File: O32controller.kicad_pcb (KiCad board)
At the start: 4 copper layers, 27 x 27 mm, 64 parts, among them J1 Conn_01x08_MountingPin, J2 BATT+, J3 BATT-, J4 Motor Connection, J5 Motor Connection, J6 Motor Connection, J7 BATT+, J8 BATT-, Q1 DMM0022A, Q2 DMM0022A, Q3 DMM0022A, U1 AS5047D, U2 STSPIN32F0A

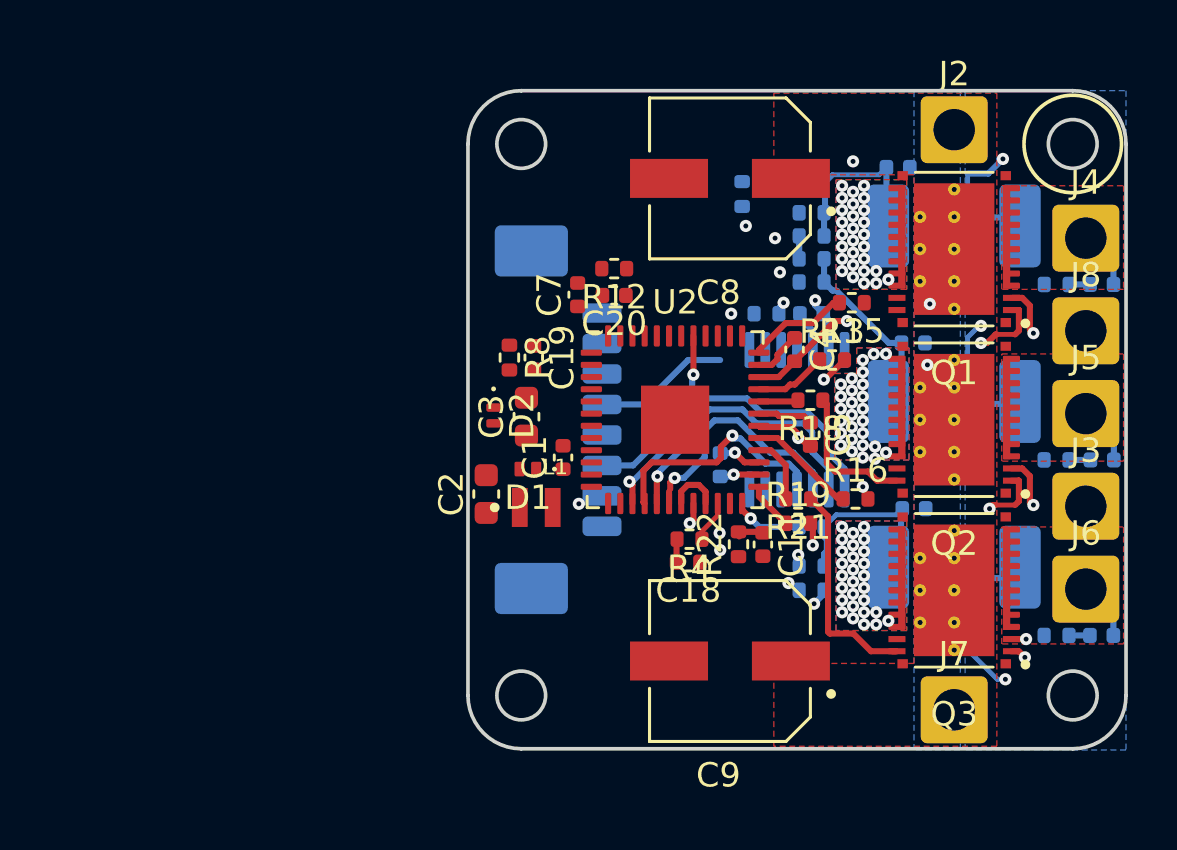
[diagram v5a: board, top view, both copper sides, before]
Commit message: just need to figure out gpio and buck
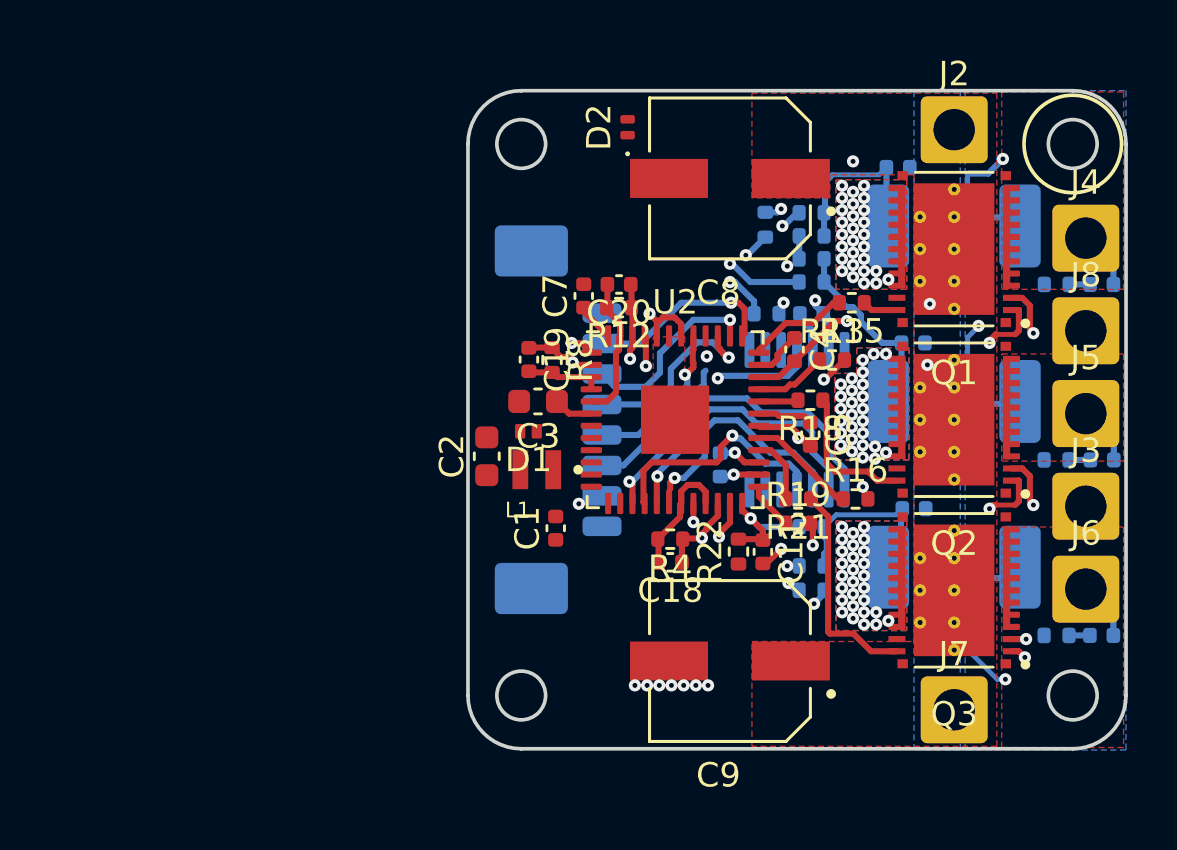
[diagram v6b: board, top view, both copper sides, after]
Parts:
- Q1, Q2, Q3: value DMM0022A -> CSD88584Q5DCT
- moved D2 13.0 mm to (43.0, 38.0), turned to 90 degrees
- moved C1 2.92 mm to (40.1, 54.5)
- moved R8 1.75 mm to (40.0, 47.5)
- moved R12 1.61 mm to (42.7, 45.4)
- moved R3 1.58 mm to (48.7, 42.0)
- moved L1 1.55 mm to (39.3, 52.0), turned to 180 degrees
- moved C2 1.55 mm to (37.3, 51.5)
- moved D1 1.55 mm to (39.0, 50.5)
- moved R4 0.79 mm to (44.8, 54.9)
- moved C3 0.79 mm to (39.4, 49.2), turned to 180 degrees
- moved C18 0.74 mm to (44.8, 55.9)
- moved C20 0.49 mm to (42.7, 44.5)
- moved C11 0.30 mm to (48.6, 55.4)
- moved R22 0.30 mm to (47.6, 55.4)
- moved C7 0.25 mm to (41.2, 44.9)
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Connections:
- J1 pad 2: I2C_SCL -> unconnected-(J1-Pad2)
- J1 pad 3: I2C_SDA -> I2C_SCL
- J1 pad 4: /GPIO_PA15 -> I2C_SDA
- J1 pad 5: SWD_CLK -> /GPIO_PA15
- J1 pad 6: SWD_IO -> SWD_CLK
- J1 pad 7: unconnected-(J1-Pad7) -> SWD_IO
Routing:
- net +3.3V: track 2.36 -> 15.3 mm, vias 0 -> 1
- net /OP_V_N: track 0.00 -> 12.9 mm, vias 0 -> 2
- net /OP_V_P: track 0.00 -> 12.0 mm, vias 0 -> 2
- net /GPIO_PA15: track 0.00 -> 8.04 mm, vias 0 -> 1
- net SWD_IO: track 0.00 -> 7.80 mm
- net I2C_SCL: track 0.00 -> 6.17 mm
- net /OP_W_O: track 0.00 -> 5.91 mm
- net /Motor phase U/Sense_N: track 10.7 -> 15.1 mm, vias 2 -> 3
- net GND: track 3.14 -> 6.77 mm, vias 2 -> 11
- net /OP_W_N: track 15.8 -> 19.1 mm, vias 1 -> 2
- net /OP_U_P: track 13.5 -> 16.7 mm
- net /OP_V_O: track 0.00 -> 3.22 mm
- net SWD_CLK: track 5.61 -> 7.74 mm, vias 0 -> 1
- net /OP_U_O: track 3.21 -> 4.95 mm
- net VBUS: track 0.00 -> 1.62 mm
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- added copper zone on F.Cu, net GND
- added copper zone on In2.Cu, net GND

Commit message: i don't like CAN
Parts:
- added REF**: SM02B-SRSS-TB_LF__SN_, O32controller:SM02B-SRSS-TB(LF)(SN), B.Cu at (40.0, 44.0)
- moved J1 19.8 mm to (21.3, 57.6)
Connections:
- net Net-(C13-Pad1) renamed /Motor phase U/Motor
- net Net-(C15-Pad1) renamed /Motor phase V/Motor
- net Net-(C17-Pad1) renamed /Motor phase W/Motor
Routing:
- net I2C_SDA: track 6.53 -> 12.7 mm
- net I2C_SCL: track 6.17 -> 0.00 mm
- net +3.3V: track 15.3 -> 17.6 mm

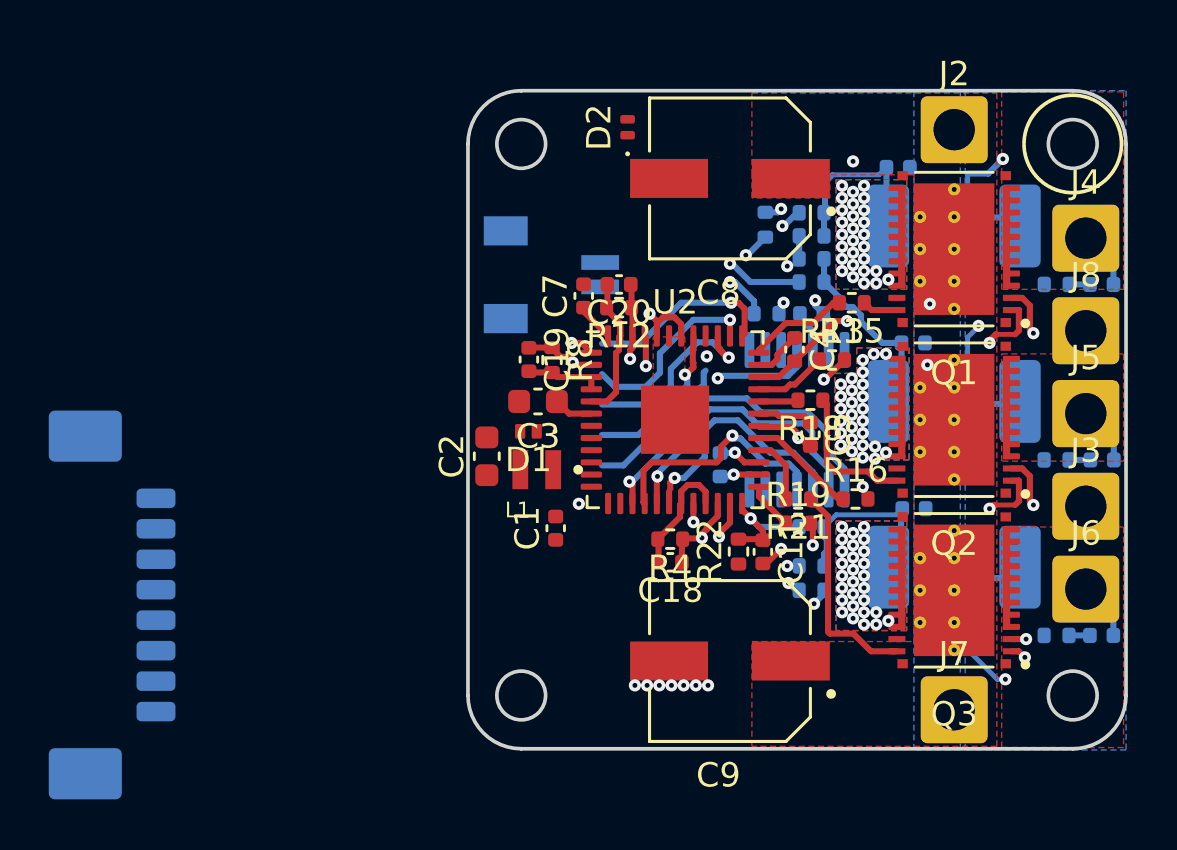
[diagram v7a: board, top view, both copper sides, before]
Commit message: assigned gpio and adcs
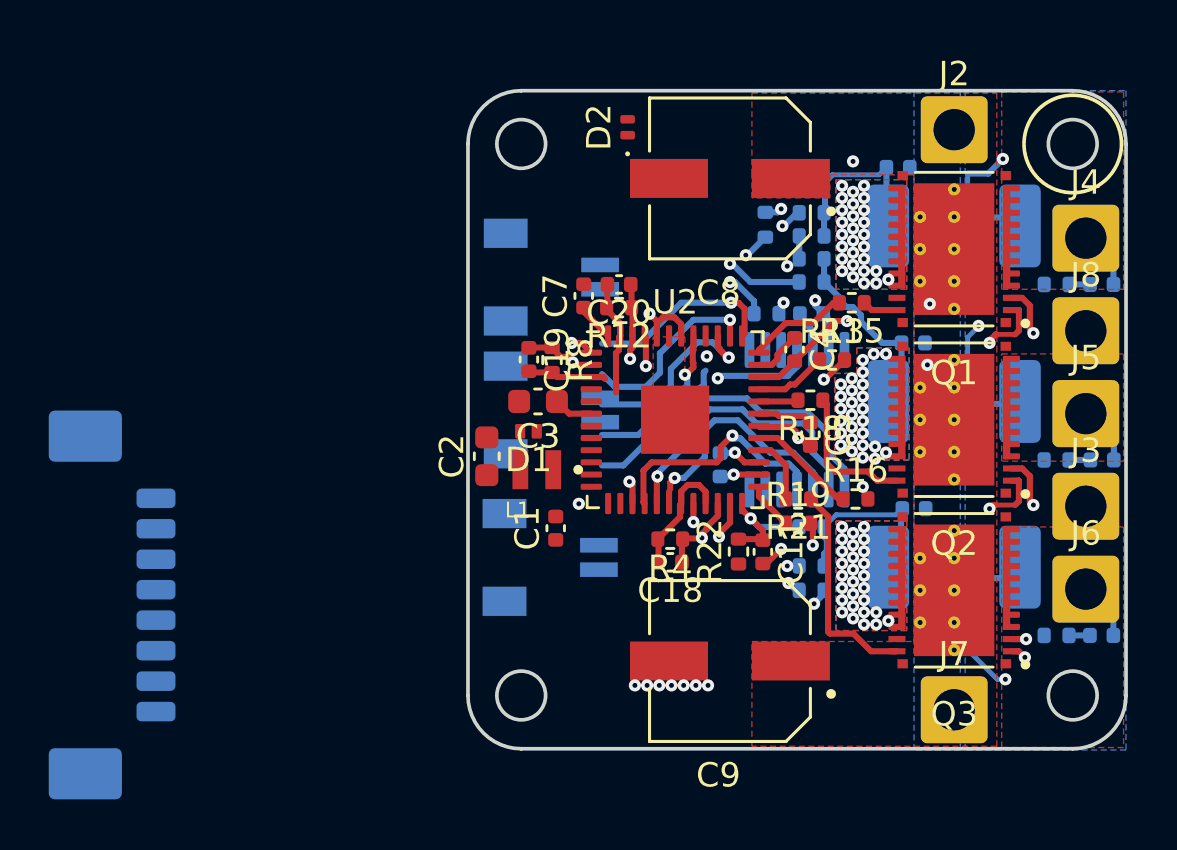
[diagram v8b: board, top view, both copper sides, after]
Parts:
- removed the REF** at (40.0, 44.0)
- added REF**: SM02B-SRSS-TB_LF__SN_, O32controller:SM02B-SRSS-TB(LF)(SN), B.Cu at (40.0, 49.6)
- added REF**: SM02B-SRSS-TB_LF__SN_, O32controller:SM02B-SRSS-TB(LF)(SN), B.Cu at (39.9, 55.6)
- added REF**: SM02B-SRSS-TB_LF__SN_, O32controller:SM02B-SRSS-TB(LF)(SN), B.Cu at (40.0, 44.1)
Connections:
- U1 pad 1: /~{MAG_CS} -> unconnected-(U1-Pad1)
- U2 pad 11: unconnected-(U2-Pad11) -> /OP_V_O
- U2 pad 12: unconnected-(U2-Pad12) -> /USART1_DE
- U2 pad 13: unconnected-(U2-Pad13) -> /USART1_TX
- U2 pad 14: unconnected-(U2-Pad14) -> /OP_W_O
- U2 pad 15: /~{MAG_CS} -> /BUS_SENSE
- U2 pad 39: /GPIO_PA15 -> /USART_RX
- U2 pad 4: /OP_V_O -> /GPIO_PF0
- U2 pad 5: /OP_W_O -> /GPIO_PF1
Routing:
- net /~{MAG_CS}: track 14.0 -> 0.00 mm, vias 1 -> 0
- net unconnected-(U1-Pad1): track 0.00 -> 9.96 mm
- net /USART_RX: track 0.00 -> 8.04 mm, vias 0 -> 1
- net /GPIO_PA15: track 8.04 -> 0.00 mm, vias 1 -> 0
- net /OP_W_O: track 5.91 -> 4.74 mm
- net /BUS_SENSE: track 0.00 -> 1.07 mm, vias 0 -> 1
